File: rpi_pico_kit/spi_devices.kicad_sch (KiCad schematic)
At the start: 20 parts, among them J6 Conn_01x08_Male, J7 Conn_01x08_Male, J8 Conn_01x08_Male, J9 Micro_SD_Card_Det, SW10 SW_Push, SW7 SW_Push, SW8 SW_Push, SW9 SW_Push, U7 MCP23S08-xSO

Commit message: changed footprints from 0805 to 0603
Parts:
- C26, C27: footprint Capacitor_SMD:C_0805_2012Metric_Pad1.18x1.45mm_HandSolder -> Capacitor_SMD:C_0603_1608Metric_Pad1.08x0.95mm_HandSolder; Supplier Part URL https://www.digikey.cz/en/products/detail/kemet/C0805C104M3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 -> (none)
- R87: footprint Resistor_SMD:R_0805_2012Metric_Pad1.20x1.40mm_HandSolder -> Resistor_SMD:R_0603_1608Metric_Pad0.98x0.95mm_HandSolder; Supplier Part URL https://www.digikey.cz/en/products/detail/yageo/RC0805FR-07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 -> (none)
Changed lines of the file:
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@@
       (effects (font (size 1.27 1.27)))
     )
-    (property "Footprint" "Resistor_SMD:R_0805_2012Metric_Pad1.20x1.40mm_HandSolder" (id 2) (at 111.76 147.828 90)
+    (property "Footprint" "Resistor_SMD:R_0603_1608Metric_Pad0.98x0.95mm_HandSolder" (id 2) (at 111.76 147.828 90)
       (effects (font (size 1.27 1.27)) hide)
     )
@@
       (effects (font (size 1.27 1.27)) hide)
     )
-    (property "Supplier Part URL" "https://www.digikey.cz/en/products/detail/yageo/RC0805FR-071KL/727444" (id 5) (at 111.76 146.05 0)
+    (property "Supplier Part URL" "" (id 5) (at 111.76 146.05 0)
       (effects (font (size 1.27 1.27)) hide)
     )
@@
       (effects (font (size 1.27 1.27)))
     )
-    (property "Footprint" "Capacitor_SMD:C_0805_2012Metric_Pad1.18x1.45mm_HandSolder" (id 2) (at 76.2 34.5948 0)
+    (property "Footprint" "Capacitor_SMD:C_0603_1608Metric_Pad1.08x0.95mm_HandSolder" (id 2) (at 76.2 34.5948 0)
       (effects (font (size 1.27 1.27)) hide)
     )
@@
       (effects (font (size 1.27 1.27)) hide)
     )
-    (property "Supplier Part URL" "https://www.digikey.cz/en/products/detail/kemet/C0805C104M3RAC7800/2211748" (id 6) (at 72.39 35.56 0)
+    (property "Supplier Part URL" "" (id 6) (at 72.39 35.56 0)
       (effects (font (size 1.27 1.27)) hide)
     )
@@
       (effects (font (size 1.27 1.27)))
     )
-    (property "Footprint" "Capacitor_SMD:C_0805_2012Metric_Pad1.18x1.45mm_HandSolder" (id 2) (at 173.99 113.3348 0)
+    (property "Footprint" "Capacitor_SMD:C_0603_1608Metric_Pad1.08x0.95mm_HandSolder" (id 2) (at 173.99 113.3348 0)
       (effects (font (size 1.27 1.27)) hide)
     )
@@
       (effects (font (size 1.27 1.27)) hide)
     )
-    (property "Supplier Part URL" "https://www.digikey.cz/en/products/detail/kemet/C0805C104M3RAC7800/2211748" (id 6) (at 170.18 114.3 0)
-      (effects (font (size 1.27 1.27)) hide)
-    )
+    (property "Supplier Part URL" "" (id 6) (at 170.18 114.3 0)
+      (effects (font (size 1.27 1.27)) hide)
+    )

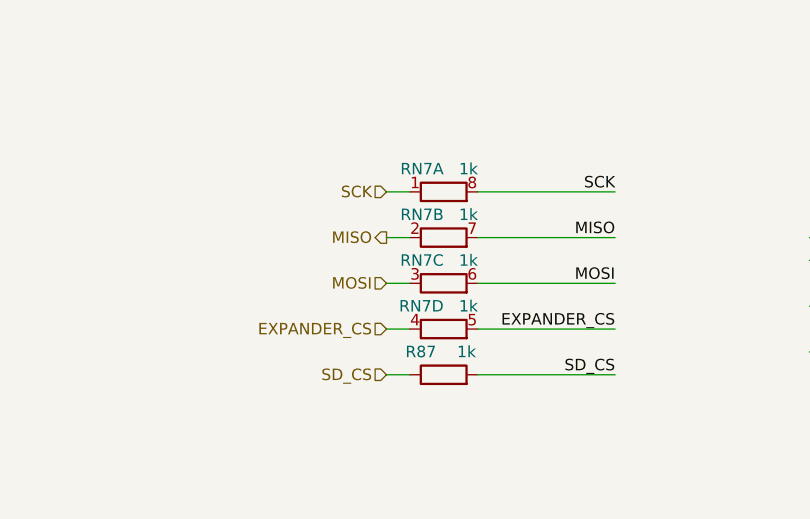
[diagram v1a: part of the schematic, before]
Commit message: SPI conflict solved
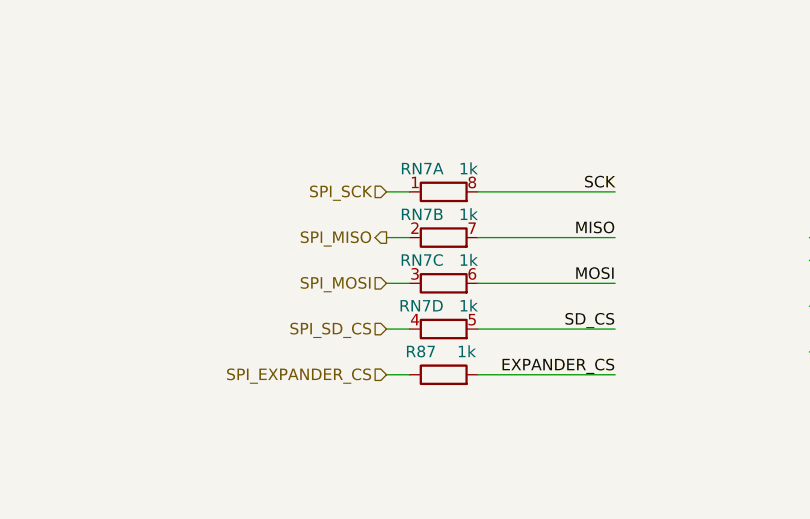
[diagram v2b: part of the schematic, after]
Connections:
- net EXPANDER_CS: now also R87.2; no longer RN7.4 (R4.1), RN7.5 (R4.2)
- net MISO: no longer RN7.2 (R2.1)
- net MOSI: no longer RN7.3 (R3.1)
- net SCK: no longer RN7.1 (R1.1)
- net SD_CS: now also RN7.5 (R4.2); no longer R87.1, R87.2
- new net SPI_EXPANDER_CS: R87.1
- new net SPI_MISO: RN7.2 (R2.1)
- new net SPI_MOSI: RN7.3 (R3.1)
- new net SPI_SCK: RN7.1 (R1.1)
- new net SPI_SD_CS: RN7.4 (R4.1)
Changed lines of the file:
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@@
   (no_connect (at 163.83 146.05))
   (no_connect (at 49.53 59.69))
+  (wire (pts (xy 237.49 64.77) (xy 240.03 64.77))
+    (stroke (width 0) (type default))
+  )
+  (wire (pts (xy 158.75 77.47) (xy 158.75 88.9))
+    (stroke (width 0) (type default))
+  )
+  (wire (pts (xy 146.05 62.23) (xy 146.05 69.85))
+    (stroke (width 0) (type default))
+  )
+  (wire (pts (xy 114.3 57.15) (xy 114.3 69.85))
+    (stroke (width 0) (type default))
+  )
+  (wire (pts (xy 105.41 54.61) (xy 105.41 69.85))
+    (stroke (width 0) (type default))
+  )
+  (wire (pts (xy 105.41 130.81) (xy 107.95 130.81))
+    (stroke (width 0) (type default))
+  )
+  (wire (pts (xy 215.9 62.23) (xy 215.9 64.77))
+    (stroke (width 0) (type default))
+  )
+  (wire (pts (xy 46.99 46.99) (xy 46.99 62.23))
+    (stroke (width 0) (type default))
+  )
+  (wire (pts (xy 133.35 59.69) (xy 179.07 59.69))
+    (stroke (width 0) (type default))
+  )
+  (wire (pts (xy 96.52 52.07) (xy 96.52 69.85))
+    (stroke (width 0) (type default))
+  )
+  (wire (pts (xy 152.4 130.81) (xy 163.83 130.81))
+    (stroke (width 0) (type default))
+  )
+  (wire (pts (xy 105.41 146.05) (xy 107.95 146.05))
+    (stroke (width 0) (type default))
+  )
+  (wire (pts (xy 49.53 69.85) (xy 46.99 69.85))
+    (stroke (width 0) (type default))
+  )
+  (wire (pts (xy 237.49 52.07) (xy 240.03 52.07))
+    (stroke (width 0) (type default))
+  )
+  (wire (pts (xy 62.23 35.56) (xy 68.58 35.56))
+    (stroke (width 0) (type default))
+  )
+  (wire (pts (xy 74.93 49.53) (xy 87.63 49.53))
+    (stroke (width 0) (type default))
+  )
+  (wire (pts (xy 114.3 86.36) (xy 114.3 88.9))
+    (stroke (width 0) (type default))
+  )
+  (wire (pts (xy 74.93 62.23) (xy 119.38 62.23))
+    (stroke (width 0) (type default))
+  )
+  (wire (pts (xy 31.75 54.61) (xy 49.53 54.61))
+    (stroke (width 0) (type default))
+  )
+  (wire (pts (xy 213.36 59.69) (xy 215.9 59.69))
+    (stroke (width 0) (type default))
+  )
+  (wire (pts (xy 133.35 27.94) (xy 133.35 33.02))
+    (stroke (width 0) (type default))
+  )
+  (wire (pts (xy 215.9 59.69) (xy 215.9 62.23))
+    (stroke (width 0) (type default))
+  )
+  (wire (pts (xy 74.93 52.07) (xy 96.52 52.07))
+    (stroke (width 0) (type default))
+  )
+  (wire (pts (xy 96.52 52.07) (xy 179.07 52.07))
+    (stroke (width 0) (type default))
+  )
+  (wire (pts (xy 161.29 151.13) (xy 163.83 151.13))
+    (stroke (width 0) (type default))
+  )
+  (wire (pts (xy 133.35 77.47) (xy 133.35 88.9))
+    (stroke (width 0) (type default))
+  )
+  (wire (pts (xy 31.75 49.53) (xy 49.53 49.53))
+    (stroke (width 0) (type default))
+  )
+  (wire (pts (xy 46.99 67.31) (xy 46.99 69.85))
+    (stroke (width 0) (type default))
+  )
+  (wire (pts (xy 161.29 135.89) (xy 161.29 114.3))
+    (stroke (width 0) (type default))
+  )
+  (wire (pts (xy 215.9 44.45) (xy 215.9 49.53))
+    (stroke (width 0) (type default))
+  )
+  (wire (pts (xy 240.03 59.69) (xy 240.03 62.23))
+    (stroke (width 0) (type default))
+  )
+  (wire (pts (xy 158.75 27.94) (xy 158.75 33.02))
+    (stroke (width 0) (type default))
+  )
+  (wire (pts (xy 158.75 64.77) (xy 158.75 69.85))
+    (stroke (width 0) (type default))
+  )
+  (wire (pts (xy 105.41 135.89) (xy 107.95 135.89))
+    (stroke (width 0) (type default))
+  )
+  (wire (pts (xy 62.23 27.94) (xy 62.23 35.56))
+    (stroke (width 0) (type default))
+  )
+  (wire (pts (xy 74.93 67.31) (xy 119.38 67.31))
+    (stroke (width 0) (type default))
+  )
+  (wire (pts (xy 87.63 49.53) (xy 179.07 49.53))
+    (stroke (width 0) (type default))
+  )
   (wire (pts (xy 115.57 140.97) (xy 130.81 140.97))
     (stroke (width 0) (type default))
   )
-  (wire (pts (xy 237.49 64.77) (xy 240.03 64.77))
-    (stroke (width 0) (type default))
-  )
-  (wire (pts (xy 158.75 77.47) (xy 158.75 88.9))
-    (stroke (width 0) (type default))
-  )
-  (wire (pts (xy 146.05 62.23) (xy 146.05 69.85))
-    (stroke (width 0) (type default))
-  )
-  (wire (pts (xy 114.3 57.15) (xy 114.3 69.85))
-    (stroke (width 0) (type default))
-  )
-  (wire (pts (xy 105.41 54.61) (xy 105.41 69.85))
-    (stroke (width 0) (type default))
-  )
-  (wire (pts (xy 105.41 130.81) (xy 107.95 130.81))
-    (stroke (width 0) (type default))
-  )
-  (wire (pts (xy 215.9 62.23) (xy 215.9 64.77))
-    (stroke (width 0) (type default))
-  )
-  (wire (pts (xy 46.99 46.99) (xy 46.99 62.23))
-    (stroke (width 0) (type default))
-  )
-  (wire (pts (xy 133.35 59.69) (xy 179.07 59.69))
-    (stroke (width 0) (type default))
-  )
-  (wire (pts (xy 96.52 52.07) (xy 96.52 69.85))
-    (stroke (width 0) (type default))
-  )
-  (wire (pts (xy 152.4 130.81) (xy 163.83 130.81))
-    (stroke (width 0) (type default))
-  )
-  (wire (pts (xy 49.53 69.85) (xy 46.99 69.85))
-    (stroke (width 0) (type default))
-  )
-  (wire (pts (xy 237.49 52.07) (xy 240.03 52.07))
-    (stroke (width 0) (type default))
-  )
-  (wire (pts (xy 62.23 35.56) (xy 68.58 35.56))
-    (stroke (width 0) (type default))
-  )
-  (wire (pts (xy 74.93 49.53) (xy 87.63 49.53))
-    (stroke (width 0) (type default))
-  )
-  (wire (pts (xy 114.3 86.36) (xy 114.3 88.9))
-    (stroke (width 0) (type default))
-  )
-  (wire (pts (xy 74.93 62.23) (xy 119.38 62.23))
-    (stroke (width 0) (type default))
-  )
-  (wire (pts (xy 31.75 54.61) (xy 49.53 54.61))
-    (stroke (width 0) (type default))
-  )
-  (wire (pts (xy 213.36 59.69) (xy 215.9 59.69))
-    (stroke (width 0) (type default))
-  )
-  (wire (pts (xy 133.35 27.94) (xy 133.35 33.02))
-    (stroke (width 0) (type default))
-  )
-  (wire (pts (xy 215.9 59.69) (xy 215.9 62.23))
-    (stroke (width 0) (type default))
-  )
-  (wire (pts (xy 74.93 52.07) (xy 96.52 52.07))
-    (stroke (width 0) (type default))
-  )
-  (wire (pts (xy 96.52 52.07) (xy 179.07 52.07))
-    (stroke (width 0) (type default))
-  )
-  (wire (pts (xy 161.29 151.13) (xy 163.83 151.13))
-    (stroke (width 0) (type default))
-  )
-  (wire (pts (xy 133.35 77.47) (xy 133.35 88.9))
-    (stroke (width 0) (type default))
-  )
-  (wire (pts (xy 31.75 49.53) (xy 49.53 49.53))
-    (stroke (width 0) (type default))
-  )
-  (wire (pts (xy 46.99 67.31) (xy 46.99 69.85))
-    (stroke (width 0) (type default))
-  )
-  (wire (pts (xy 161.29 135.89) (xy 161.29 114.3))
-    (stroke (width 0) (type default))
-  )
-  (wire (pts (xy 215.9 44.45) (xy 215.9 49.53))
-    (stroke (width 0) (type default))
-  )
-  (wire (pts (xy 240.03 59.69) (xy 240.03 62.23))
-    (stroke (width 0) (type default))
-  )
-  (wire (pts (xy 158.75 27.94) (xy 158.75 33.02))
-    (stroke (width 0) (type default))
-  )
-  (wire (pts (xy 158.75 64.77) (xy 158.75 69.85))
-    (stroke (width 0) (type default))
-  )
-  (wire (pts (xy 105.41 135.89) (xy 107.95 135.89))
-    (stroke (width 0) (type default))
-  )
-  (wire (pts (xy 62.23 27.94) (xy 62.23 35.56))
-    (stroke (width 0) (type default))
-  )
-  (wire (pts (xy 74.93 67.31) (xy 119.38 67.31))
-    (stroke (width 0) (type default))
-  )
-  (wire (pts (xy 87.63 49.53) (xy 179.07 49.53))
-    (stroke (width 0) (type default))
-  )
   (wire (pts (xy 215.9 54.61) (xy 215.9 57.15))
     (stroke (width 0) (type default))
@@
     (stroke (width 0) (type default))
   )
+  (wire (pts (xy 115.57 146.05) (xy 130.81 146.05))
+    (stroke (width 0) (type default))
+  )
   (wire (pts (xy 87.63 49.53) (xy 87.63 69.85))
     (stroke (width 0) (type default))
@@
     (stroke (width 0) (type default))
   )
-  (wire (pts (xy 115.57 146.05) (xy 130.81 146.05))
-    (stroke (width 0) (type default))
-  )
   (wire (pts (xy 158.75 43.18) (xy 158.75 64.77))
     (stroke (width 0) (type default))
@@
   )
   (wire (pts (xy 115.57 130.81) (xy 130.81 130.81))
-    (stroke (width 0) (type default))
-  )
-  (wire (pts (xy 105.41 146.05) (xy 107.95 146.05))
     (stroke (width 0) (type default))
   )
@@
     (effects (font (size 1.27 1.27)) (justify left bottom))
   )
-  (label "EXPANDER_CS" (at 130.81 140.97 0) (fields_autoplaced)
+  (label "EXPANDER_CS" (at 130.81 146.05 0) (fields_autoplaced)
     (effects (font (size 1.27 1.27)) (justify right bottom))
   )
@@
     (effects (font (size 1.27 1.27)) (justify left bottom))
   )
-  (label "SD_CS" (at 130.81 146.05 0) (fields_autoplaced)
+  (label "SD_CS" (at 130.81 140.97 0) (fields_autoplaced)
     (effects (font (size 1.27 1.27)) (justify right bottom))
   )
@@
     (effects (font (size 1.27 1.27)) (justify left bottom))
   )
-  (hierarchical_label "SCK" (shape input) (at 105.41 125.73 180) (fields_autoplaced)
+  (hierarchical_label "SPI_SCK" (shape input) (at 105.41 125.73 180) (fields_autoplaced)
     (effects (font (size 1.27 1.27)) (justify right))
   )
-  (hierarchical_label "EXPANDER_CS" (shape input) (at 105.41 140.97 180) (fields_autoplaced)
+  (hierarchical_label "SPI_EXPANDER_CS" (shape input) (at 105.41 146.05 180) (fields_autoplaced)
     (effects (font (size 1.27 1.27)) (justify right))
   )
-  (hierarchical_label "SD_CS" (shape input) (at 105.41 146.05 180) (fields_autoplaced)
+  (hierarchical_label "SPI_SD_CS" (shape input) (at 105.41 140.97 180) (fields_autoplaced)
     (effects (font (size 1.27 1.27)) (justify right))
   )
-  (hierarchical_label "MISO" (shape output) (at 105.41 130.81 180) (fields_autoplaced)
+  (hierarchical_label "SPI_MISO" (shape output) (at 105.41 130.81 180) (fields_autoplaced)
     (effects (font (size 1.27 1.27)) (justify right))
   )
-  (hierarchical_label "MOSI" (shape input) (at 105.41 135.89 180) (fields_autoplaced)
+  (hierarchical_label "SPI_MOSI" (shape input) (at 105.41 135.89 180) (fields_autoplaced)
     (effects (font (size 1.27 1.27)) (justify right))
   )

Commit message: changed footprints for resistor arrays
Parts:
- RN4, RN5, RN6, RN7: footprint Resistor_SMD:R_Array_Convex_4x1206 -> Resistor_SMD:R_Array_Convex_4x0603
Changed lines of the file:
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@@
       (effects (font (size 1.27 1.27)) (justify right))
     )
-    (property "Footprint" "Resistor_SMD:R_Array_Convex_4x1206" (id 2) (at 116.332 73.66 90)
+    (property "Footprint" "Resistor_SMD:R_Array_Convex_4x0603" (id 2) (at 116.332 73.66 90)
       (effects (font (size 1.27 1.27)) hide)
     )
@@
       (effects (font (size 1.27 1.27)) (justify right))
     )
-    (property "Footprint" "Resistor_SMD:R_Array_Convex_4x1206" (id 2) (at 123.19 57.658 90)
+    (property "Footprint" "Resistor_SMD:R_Array_Convex_4x0603" (id 2) (at 123.19 57.658 90)
       (effects (font (size 1.27 1.27)) hide)
     )
@@
       (effects (font (size 1.27 1.27)) (justify right))
     )
-    (property "Footprint" "Resistor_SMD:R_Array_Convex_4x1206" (id 2) (at 135.382 73.66 90)
+    (property "Footprint" "Resistor_SMD:R_Array_Convex_4x0603" (id 2) (at 135.382 73.66 90)
       (effects (font (size 1.27 1.27)) hide)
     )
@@
       (effects (font (size 1.27 1.27)) (justify right))
     )
-    (property "Footprint" "Resistor_SMD:R_Array_Convex_4x1206" (id 2) (at 89.662 73.66 90)
+    (property "Footprint" "Resistor_SMD:R_Array_Convex_4x0603" (id 2) (at 89.662 73.66 90)
       (effects (font (size 1.27 1.27)) hide)
     )
@@
       (effects (font (size 1.27 1.27)) (justify right))
     )
-    (property "Footprint" "Resistor_SMD:R_Array_Convex_4x1206" (id 2) (at 111.76 123.698 90)
+    (property "Footprint" "Resistor_SMD:R_Array_Convex_4x0603" (id 2) (at 111.76 123.698 90)
       (effects (font (size 1.27 1.27)) hide)
     )
@@
       (effects (font (size 1.27 1.27)) (justify right))
     )
-    (property "Footprint" "Resistor_SMD:R_Array_Convex_4x1206" (id 2) (at 123.19 62.738 90)
+    (property "Footprint" "Resistor_SMD:R_Array_Convex_4x0603" (id 2) (at 123.19 62.738 90)
       (effects (font (size 1.27 1.27)) hide)
     )
@@
       (effects (font (size 1.27 1.27)) (justify right))
     )
-    (property "Footprint" "Resistor_SMD:R_Array_Convex_4x1206" (id 2) (at 111.76 128.778 90)
+    (property "Footprint" "Resistor_SMD:R_Array_Convex_4x0603" (id 2) (at 111.76 128.778 90)
       (effects (font (size 1.27 1.27)) hide)
     )
@@
       (effects (font (size 1.27 1.27)) (justify right))
     )
-    (property "Footprint" "Resistor_SMD:R_Array_Convex_4x1206" (id 2) (at 173.482 73.66 90)
+    (property "Footprint" "Resistor_SMD:R_Array_Convex_4x0603" (id 2) (at 173.482 73.66 90)
       (effects (font (size 1.27 1.27)) hide)
     )
@@
       (effects (font (size 1.27 1.27)) (justify right))
     )
-    (property "Footprint" "Resistor_SMD:R_Array_Convex_4x1206" (id 2) (at 123.19 60.198 90)
+    (property "Footprint" "Resistor_SMD:R_Array_Convex_4x0603" (id 2) (at 123.19 60.198 90)
       (effects (font (size 1.27 1.27)) hide)
     )
@@
       (effects (font (size 1.27 1.27)) (justify right))
     )
-    (property "Footprint" "Resistor_SMD:R_Array_Convex_4x1206" (id 2) (at 111.76 138.938 90)
+    (property "Footprint" "Resistor_SMD:R_Array_Convex_4x0603" (id 2) (at 111.76 138.938 90)
       (effects (font (size 1.27 1.27)) hide)
     )
@@
       (effects (font (size 1.27 1.27)) (justify right))
     )
-    (property "Footprint" "Resistor_SMD:R_Array_Convex_4x1206" (id 2) (at 148.082 73.66 90)
+    (property "Footprint" "Resistor_SMD:R_Array_Convex_4x0603" (id 2) (at 148.082 73.66 90)
       (effects (font (size 1.27 1.27)) hide)
     )
@@
       (effects (font (size 1.27 1.27)) (justify right))
     )
-    (property "Footprint" "Resistor_SMD:R_Array_Convex_4x1206" (id 2) (at 98.552 73.66 90)
+    (property "Footprint" "Resistor_SMD:R_Array_Convex_4x0603" (id 2) (at 98.552 73.66 90)
       (effects (font (size 1.27 1.27)) hide)
     )
@@
       (effects (font (size 1.27 1.27)) (justify right))
     )
-    (property "Footprint" "Resistor_SMD:R_Array_Convex_4x1206" (id 2) (at 107.442 73.66 90)
+    (property "Footprint" "Resistor_SMD:R_Array_Convex_4x0603" (id 2) (at 107.442 73.66 90)
       (effects (font (size 1.27 1.27)) hide)
     )
@@
       (effects (font (size 1.27 1.27)) (justify right))
     )
-    (property "Footprint" "Resistor_SMD:R_Array_Convex_4x1206" (id 2) (at 111.76 133.858 90)
+    (property "Footprint" "Resistor_SMD:R_Array_Convex_4x0603" (id 2) (at 111.76 133.858 90)
       (effects (font (size 1.27 1.27)) hide)
     )
@@
       (effects (font (size 1.27 1.27)) (justify right))
     )
-    (property "Footprint" "Resistor_SMD:R_Array_Convex_4x1206" (id 2) (at 123.19 65.278 90)
+    (property "Footprint" "Resistor_SMD:R_Array_Convex_4x0603" (id 2) (at 123.19 65.278 90)
       (effects (font (size 1.27 1.27)) hide)
     )
@@
       (effects (font (size 1.27 1.27)) (justify right))
     )
-    (property "Footprint" "Resistor_SMD:R_Array_Convex_4x1206" (id 2) (at 160.782 73.66 90)
-      (effects (font (size 1.27 1.27)) hide)
-    )
+    (property "Footprint" "Resistor_SMD:R_Array_Convex_4x0603" (id 2) (at 160.782 73.66 90)
+      (effects (font (size 1.27 1.27)) hide)
+    )
